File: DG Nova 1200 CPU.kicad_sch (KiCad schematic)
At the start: 239 parts, among them Q1 MPS3640, U1 74LS122, U10 74LS20, U100 045, U101 74LS04, U102 74LS179, U103 74LS179, U105 74LS179, U106 74LS179, U107 74LS179, U108 74LS179, U109 74LS00, U11 74LS03, U110 74LS20, U111 74LS10, U112 74LS51, U113 74LS114, U114 74LS51, U115 74LS179, U116 74LS157, U117 74LS181, U118 74LS00, U119 74LS170, U12 74LS00, U120 8264, U121 74LS157, U122 74LS179, U123 8225, U124 8225, U125 8264, U13 045, U14 74LS20, U15 74LS20, U16 74LS04, U17 74LS179, U18 74LS20, U19 74LS00, U2 74LS74, U20 74LS74, U21 74LS00, U22 74LS04, U23 74LS179, U24 74LS51, U25 74LS139, U26 74LS04, U27 74LS04, U28 74LS179, U29 74LS179, U3 74LS00, U30 82S23, U31 82S23, U32 74LS179, U33 74LS179, U34 045, U35 74LS10, U36 74LS00, U37 74LS179, U38 74LS179, U39 74LS179, U4 045, U40 74LS179, U41 045, U42 74LS179, U43 74H54, U44 74LS51, U45 74LS51, U46 74H54, U47 74H54, U48 045, U49 74LS03, U5 74LS04, U50 74LS10, U51 74LS139, U52 74LS139, U53 045, U54 74LS179, U55 74LS51, U56 74LS20, U57 74LS00, U58 045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

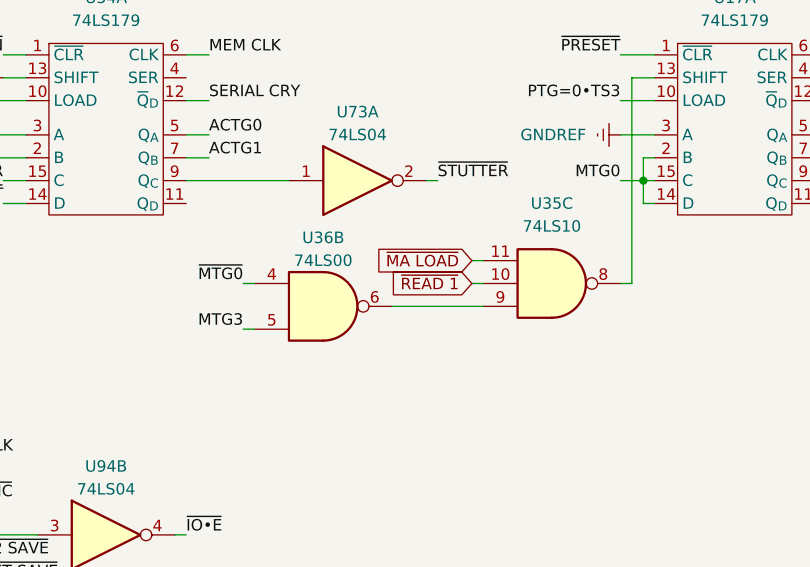
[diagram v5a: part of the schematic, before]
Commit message: Fixed read1 label
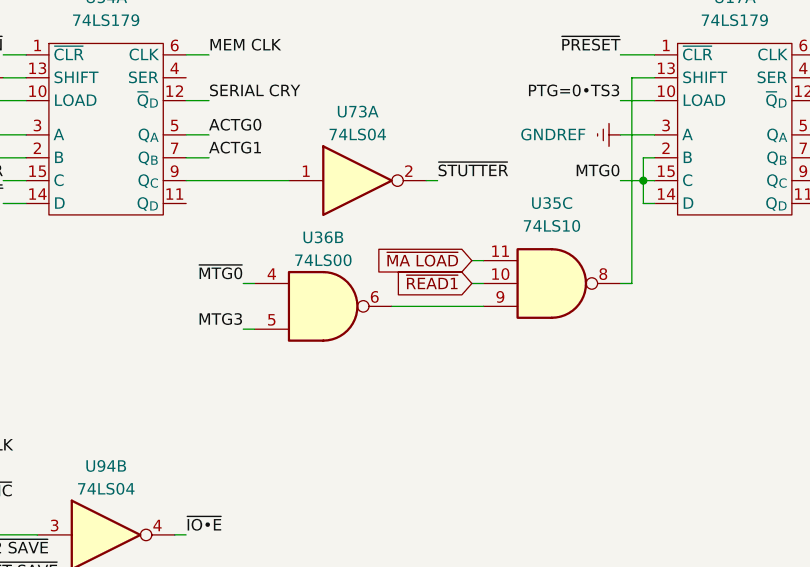
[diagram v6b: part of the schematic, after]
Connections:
- net ~{READ 1} is gone; now on net ~{READ1}: U35.10
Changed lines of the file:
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@@
 		)
 	)
-	(global_label "~{READ 1}"
+	(global_label "~{READ1}"
 		(shape input)
 		(at 124.46 45.72 180)
@@
 		)
 		(property "Intersheetrefs" "${INTERSHEET_REFS}"
-			(at 115.0921 45.6406 0)
+			(at 115.4877 45.72 0)
 			(effects
 				(font

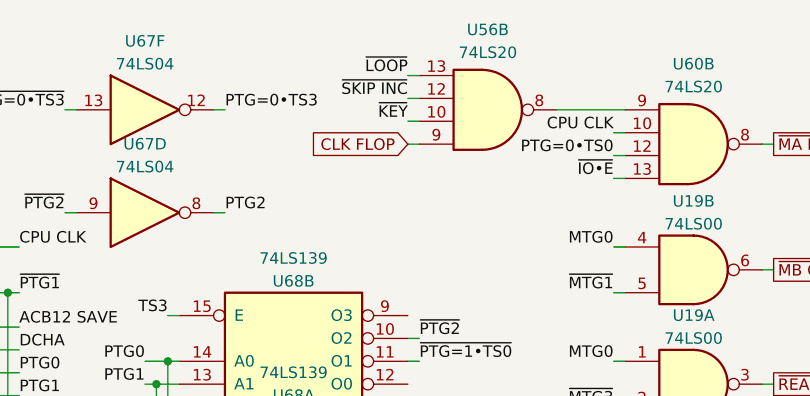
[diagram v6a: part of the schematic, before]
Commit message: Fixed pins 9 and 10 in U56
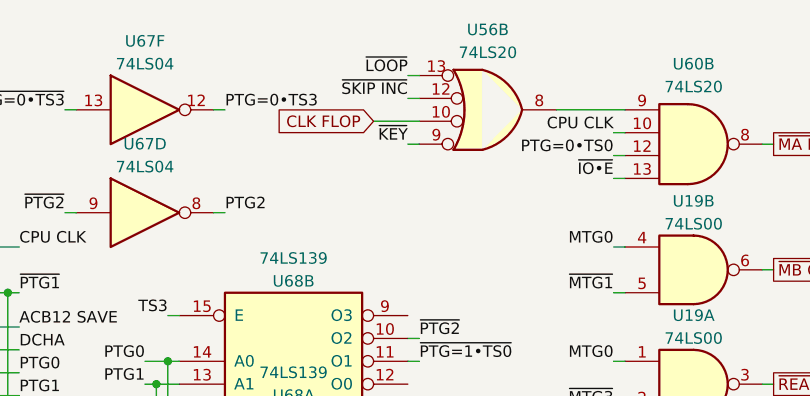
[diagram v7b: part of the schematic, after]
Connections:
- net CLK FLOP: now also U56.10; no longer U56.9
- net ~{KEY}: now also U56.9; no longer U56.10
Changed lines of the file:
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@@
 	(wire
 		(pts
+			(xy 340.36 25.4) (xy 341.63 25.4)
+		)
+		(stroke
+			(width 0)
+			(type default)
+		)
+	)
+	(wire
+		(pts
 			(xy 229.87 243.84) (xy 231.14 243.84)
 		)
@@
 	(wire
 		(pts
+			(xy 336.55 22.86) (xy 341.63 22.86)
+		)
+		(stroke
+			(width 0)
+			(type default)
+		)
+	)
+	(wire
+		(pts
 			(xy 596.9 190.5) (xy 598.17 190.5)
 		)
@@
 	(wire
 		(pts
-			(xy 340.36 25.4) (xy 341.63 25.4)
-		)
-		(stroke
-			(width 0)
-			(type default)
-		)
-	)
-	(wire
-		(pts
 			(xy 840.74 266.7) (xy 839.47 266.7)
 		)
@@
 	(wire
 		(pts
-			(xy 340.36 22.86) (xy 341.63 22.86)
-		)
-		(stroke
-			(width 0)
-			(type default)
-		)
-	)
-	(wire
-		(pts
 			(xy 345.44 326.39) (xy 337.82 326.39)
 		)
@@
 	)
 	(label "~{KEY}"
-		(at 340.36 22.86 180)
-		(effects
-			(font
-				(size 1.27 1.27)
-			)
-			(justify right bottom)
-		)
-	)
-	(label "~{KEY}"
 		(at 516.89 83.82 180)
 		(effects
@@
 		)
 	)
+	(label "~{KEY}"
+		(at 340.36 25.4 180)
+		(effects
+			(font
+				(size 1.27 1.27)
+			)
+			(justify right bottom)
+		)
+	)
 	(label "MTG2"
 		(at 165.1 34.29 0)
@@
 		)
 	)
-	(global_label "CLK FLOP"
-		(shape input)
-		(at 340.36 25.4 180)
-		(fields_autoplaced yes)
-		(effects
-			(font
-				(size 1.27 1.27)
-			)
-			(justify right)
-		)
-		(property "Intersheetrefs" "${INTERSHEET_REFS}"
-			(at 328.694 25.3206 0)
-			(effects
-				(font
-					(size 1.27 1.27)
-				)
-				(justify right)
-				(hide yes)
-			)
-		)
-	)
 	(global_label "~{READ IO}"
 		(shape output)
@@
 		)
 	)
+	(global_label "CLK FLOP"
+		(shape input)
+		(at 336.55 22.86 180)
+		(fields_autoplaced yes)
+		(effects
+			(font
+				(size 1.27 1.27)
+			)
+			(justify right)
+		)
+		(property "Intersheetrefs" "${INTERSHEET_REFS}"
+			(at 324.884 22.7806 0)
+			(effects
+				(font
+					(size 1.27 1.27)
+				)
+				(justify right)
+				(hide yes)
+			)
+		)
+	)
 	(global_label "MB LOAD"
 		(shape output)
@@
 		(mirror x)
 		(unit 2)
+		(convert 2)
 		(exclude_from_sim no)
 		(in_bom yes)

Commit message: Fixed misslabeling
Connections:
- net D+ESET+~{TS3} is gone; now on net (D+E SET)+~{TS3}: U24.13
- net ~{MBC8}: now also U11.9
- net ~{MBC9}: no longer U11.9
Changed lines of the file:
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@@
 		)
 	)
-	(label "~{MBC9}"
+	(label "~{MBC8}"
 		(at 659.13 142.24 180)
 		(effects
@@
 		)
 	)
-	(label "D+ESET+~{TS3}"
+	(label "(D+E SET)+~{TS3}"
 		(at 93.98 177.8 270)
 		(effects
